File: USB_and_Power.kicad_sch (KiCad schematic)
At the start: 33 parts, among them J2 USB_C_Receptacle_USB2.0_14P, U2 TLV61070ADBV, U3 BQ24074RGT, U4 82400102, U5 TPS63031DSK, U6 FUSB303BTMX

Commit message: Added layout
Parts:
- removed J2: USB_C_Receptacle_USB2.0_14P, Connector_USB:USB_C_Receptacle_GCT_USB4105-xx-A_16P_TopMnt_Horizontal, symbol Connector:USB_C_Receptacle_USB2.0_14P
- added J6: USB_C_Receptacle_USB2.0_16P, Connector_USB:USB_C_Receptacle_GCT_USB4105-xx-A_16P_TopMnt_Horizontal, symbol Connector:USB_C_Receptacle_USB2.0_16P
- U2: footprint Package_DFN_QFN:Texas_RWU0007A_VQFN-7_2x2mm_P0.5mm -> TLV61070A:SOT95P280X145-6N
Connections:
- net GND: now also J6.A1 (GND), J6.A12 (GND), J6.B1 (GND), J6.B12 (GND)
- net VBUS: now also J6.A4 (VBUS), J6.A9 (VBUS), J6.B4 (VBUS), J6.B9 (VBUS)
- net at U6.1 (CC1): now also J6.A5 (CC1)
- net at U4.6: now also J6.A6 (D+), J6.B6 (D+)
- net at U4.4: now also J6.A7 (D-), J6.B7 (D-)
- net at U6.2 (CC2): now also J6.B5 (CC2)
- net at C17.1, R9.2: now also J6.S1 (SHIELD)
- no-connect marks 2 -> 4
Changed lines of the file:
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@@
 	)
 	(no_connect
+		(at 24.13 110.49)
+	)
+	(no_connect
 		(at 114.3 154.94)
 	)
 	(no_connect
+		(at 24.13 107.95)
+	)
+	(no_connect
 		(at 114.3 152.4)
 	)
@@
 	)
 	(symbol
-		(lib_id "power:GND")
-		(at 115.57 130.81 0)
+		(lib_name "USB_C_Receptacle_USB2.0_16P_1")
+		(lib_id "Connector:USB_C_Receptacle_USB2.0_16P")
+		(at 39.37 105.41 0)
 		(unit 1)
 		(exclude_from_sim no)
@@
 		(dnp no)
 		(fields_autoplaced yes)
-		(property "Reference" "#PWR020"
-			(at 115.57 137.16 0)
+		(property "Reference" "J6"
+			(at 39.37 74.93 0)
 			(effects
 				(font
 					(size 1.27 1.27)
 				)
-				(hide yes)
 			)
 		)
-		(property "Value" "GND"
-			(at 115.57 135.89 0)
+		(property "Value" "USB_C_Receptacle_USB2.0_16P"
+			(at 39.37 77.47 0)
 			(effects
 				(font
@@
 			)
 		)
-		(property "Footprint" ""
-			(at 115.57 130.81 0)
+		(property "Footprint" "Connector_USB:USB_C_Receptacle_GCT_USB4105-xx-A_16P_TopMnt_Horizontal"
+			(at 43.18 105.41 0)
 			(effects
 				(font
@@
 			)
 		)
-		(property "Datasheet" ""
-			(at 115.57 130.81 0)
+		(property "Datasheet" "https://www.usb.org/sites/default/files/documents/usb_type-c.zip"
+			(at 20.574 139.954 0)
 			(effects
 				(font
@@
 			)
 		)
-		(property "Description" "Power symbol creates a global label with name \"GND\" , ground"
-			(at 115.57 130.81 0)
+		(property "Description" "USB 2.0-only 16P Type-C Receptacle connector"
+			(at 39.37 114.3 0)
 			(effects
 				(font
@@
 			)
 		)
-		(pin "1"
+		(pin "B5"
+		)
+		(pin "A6"
+		)
+		(pin "A5"
+		)
+		(pin "A8"
+		)
+		(pin "B12"
+		)
+		(pin "A4"
+		)
+		(pin "A9"
+		)
+		(pin "B6"
+		)
+		(pin "B1"
+		)
+		(pin "A7"
+		)
+		(pin "S1"
+		)
+		(pin "B8"
+		)
+		(pin "B4"
+		)
+		(pin "B9"
+		)
+		(pin "A12"
+		)
+		(pin "B7"
+		)
+		(pin "A1"
 		)
 		(instances
 			(project "Snail_v1"
 				(path "/98695d9f-8521-4f7d-bb41-f22c1215a8e7/de25fb69-79bf-4de2-a7cc-36507c8760b8"
-					(reference "#PWR020")
+					(reference "J6")
 					(unit 1)
 				)
@@
 	(symbol
 		(lib_id "power:GND")
-		(at 142.24 68.58 0)
+		(at 115.57 130.81 0)
 		(unit 1)
 		(exclude_from_sim no)
@@
 		(dnp no)
 		(fields_autoplaced yes)
-		(property "Reference" "#PWR012"
-			(at 142.24 74.93 0)
+		(property "Reference" "#PWR020"
+			(at 115.57 137.16 0)
 			(effects
 				(font
@@
 		)
 		(property "Value" "GND"
-			(at 142.24 73.66 0)
+			(at 115.57 135.89 0)
 			(effects
 				(font
@@
 		)
 		(property "Footprint" ""
-			(at 142.24 68.58 0)
+			(at 115.57 130.81 0)
 			(effects
 				(font
@@
 		)
 		(property "Datasheet" ""
-			(at 142.24 68.58 0)
+			(at 115.57 130.81 0)
 			(effects
 				(font
@@
 		)
 		(property "Description" "Power symbol creates a global label with name \"GND\" , ground"
-			(at 142.24 68.58 0)
+			(at 115.57 130.81 0)
 			(effects
 				(font
@@
 			(project "Snail_v1"
 				(path "/98695d9f-8521-4f7d-bb41-f22c1215a8e7/de25fb69-79bf-4de2-a7cc-36507c8760b8"
-					(reference "#PWR012")
+					(reference "#PWR020")
 					(unit 1)
 				)
@@
 	)
 	(symbol
-		(lib_id "Device:C_Small")
-		(at 73.66 88.9 0)
-		(mirror x)
+		(lib_id "power:GND")
+		(at 142.24 68.58 0)
 		(unit 1)
 		(exclude_from_sim no)
@@
 		(dnp no)
 		(fields_autoplaced yes)
-		(property "Reference" "C10"
-			(at 71.12 87.6235 0)
+		(property "Reference" "#PWR012"
+			(at 142.24 74.93 0)
 			(effects
 				(font
 					(size 1.27 1.27)
 				)
-				(justify right)
+				(hide yes)
 			)
 		)
-		(property "Value" "1uF"
-			(at 71.12 90.1635 0)
+		(property "Value" "GND"
+			(at 142.24 73.66 0)
 			(effects
 				(font
 					(size 1.27 1.27)
 				)
-				(justify right)
 			)
 		)
-		(property "Footprint" "Capacitor_SMD:C_0805_2012Metric_Pad1.18x1.45mm_HandSolder"
-			(at 73.66 88.9 0)
+		(property "Footprint" ""
+			(at 142.24 68.58 0)
 			(effects
 				(font
@@
 			)
 		)
-		(property "Datasheet" "~"
-			(at 73.66 88.9 0)
+		(property "Datasheet" ""
+			(at 142.24 68.58 0)
 			(effects
 				(font
@@
 			)
 		)
-		(property "Description" "Unpolarized capacitor, small symbol"
-			(at 73.66 88.9 0)
+		(property "Description" "Power symbol creates a global label with name \"GND\" , ground"
+			(at 142.24 68.58 0)
 			(effects
 				(font
@@
 			)
 		)
-		(pin "2"
-		)
 		(pin "1"
 		)
@@
 			(project "Snail_v1"
 				(path "/98695d9f-8521-4f7d-bb41-f22c1215a8e7/de25fb69-79bf-4de2-a7cc-36507c8760b8"
-					(reference "C10")
+					(reference "#PWR012")
 					(unit 1)
 				)
@@
 	)
 	(symbol
-		(lib_id "Connector:USB_C_Receptacle_USB2.0_14P")
-		(at 39.37 105.41 0)
+		(lib_id "Device:C_Small")
+		(at 73.66 88.9 0)
+		(mirror x)
 		(unit 1)
 		(exclude_from_sim no)
@@
 		(on_board yes)
 		(dnp no)
-		(property "Reference" "J2"
-			(at 39.37 75.946 0)
+		(fields_autoplaced yes)
+		(property "Reference" "C10"
+			(at 71.12 87.6235 0)
 			(effects
 				(font
 					(size 1.27 1.27)
 				)
+				(justify right)
 			)
 		)
-		(property "Value" "USB_C_Receptacle_USB2.0_14P"
-			(at 39.37 78.486 0)
+		(property "Value" "1uF"
+			(at 71.12 90.1635 0)
 			(effects
 				(font
 					(size 1.27 1.27)
 				)
+				(justify right)
 			)
 		)
-		(property "Footprint" "Connector_USB:USB_C_Receptacle_GCT_USB4105-xx-A_16P_TopMnt_Horizontal"
-			(at 43.18 105.41 0)
+		(property "Footprint" "Capacitor_SMD:C_0805_2012Metric_Pad1.18x1.45mm_HandSolder"
+			(at 73.66 88.9 0)
 			(effects
 				(font
@@
 			)
 		)
-		(property "Datasheet" "https://www.usb.org/sites/default/files/documents/usb_type-c.zip"
-			(at 43.18 106.68 0)
+		(property "Datasheet" "~"
+			(at 73.66 88.9 0)
 			(effects
 				(font
@@
 			)
 		)
-		(property "Description" "USB 2.0-only 14P Type-C Receptacle connector"
-			(at 39.37 106.68 0)
+		(property "Description" "Unpolarized capacitor, small symbol"
+			(at 73.66 88.9 0)
 			(effects
 				(font
@@
 			)
 		)
-		(pin "B7"
-		)
-		(pin "B6"
-		)
-		(pin "S1"
-		)
-		(pin "A1"
-		)
-		(pin "A4"
-		)
-		(pin "A9"
-		)
-		(pin "B4"
-		)
-		(pin "A7"
-		)
-		(pin "B1"
-		)
-		(pin "B12"
-		)
-		(pin "B9"
-		)
-		(pin "A5"
-		)
-		(pin "B5"
-		)
-		(pin "A12"
+		(pin "2"
 		)
-		(pin "A6"
+		(pin "1"
 		)
 		(instances
 			(project "Snail_v1"
 				(path "/98695d9f-8521-4f7d-bb41-f22c1215a8e7/de25fb69-79bf-4de2-a7cc-36507c8760b8"
-					(reference "J2")
+					(reference "C10")
 					(unit 1)
 				)
@@
 			)
 		)
-		(property "Footprint" "Package_DFN_QFN:Texas_RWU0007A_VQFN-7_2x2mm_P0.5mm"
+		(property "Footprint" "TLV61070A:SOT95P280X145-6N"
 			(at 228.6 58.42 0)
 			(effects

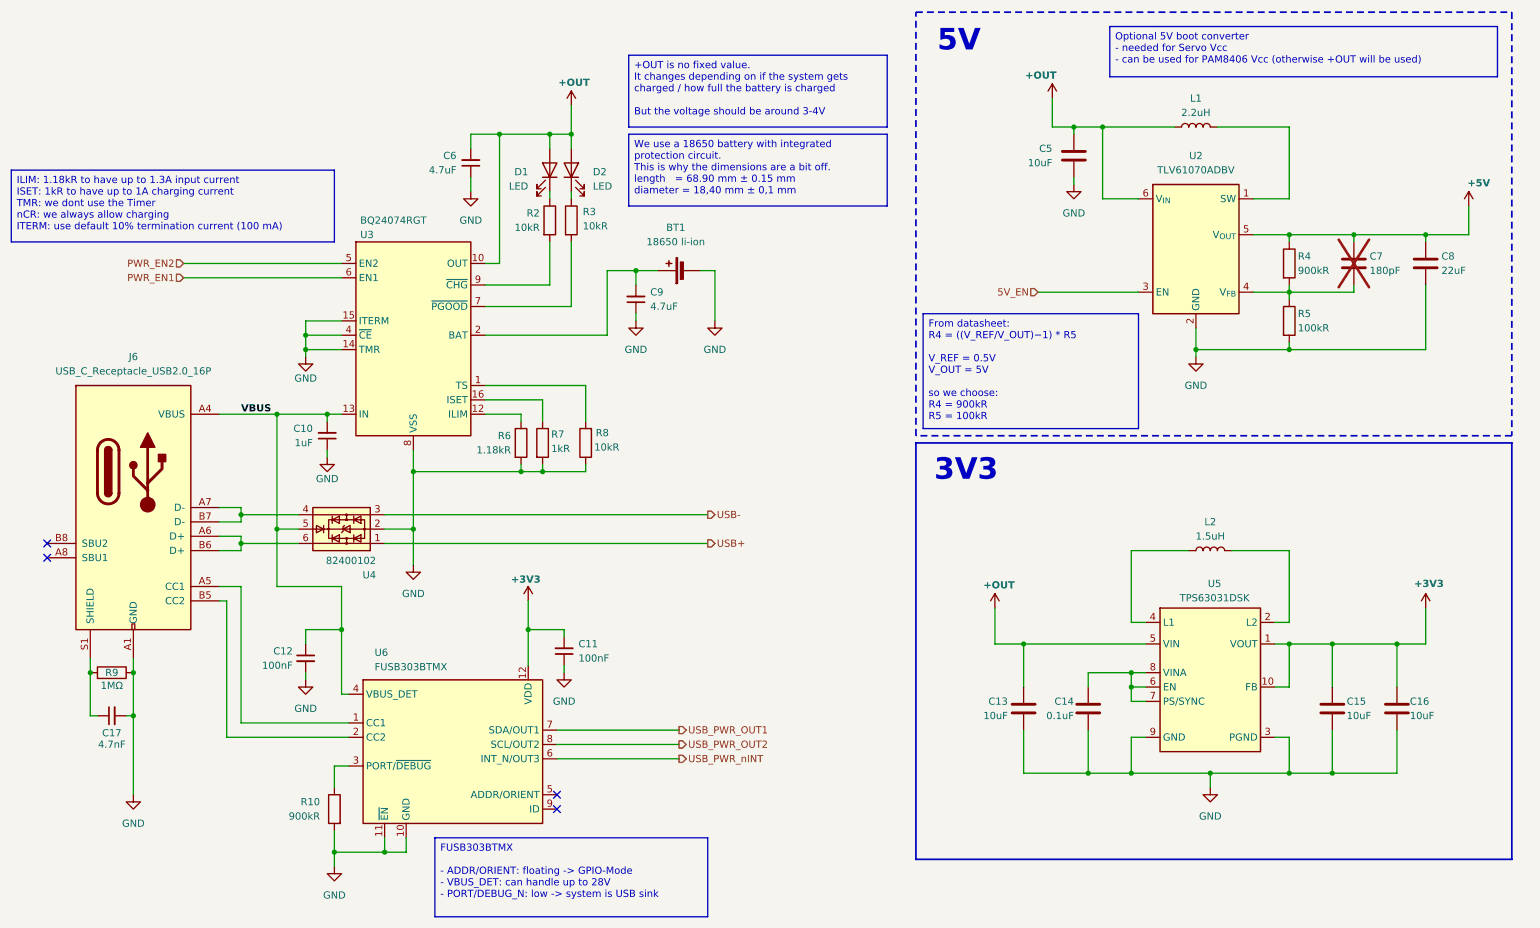
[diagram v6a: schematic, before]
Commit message: Did Silkscreen + added images of PCBA
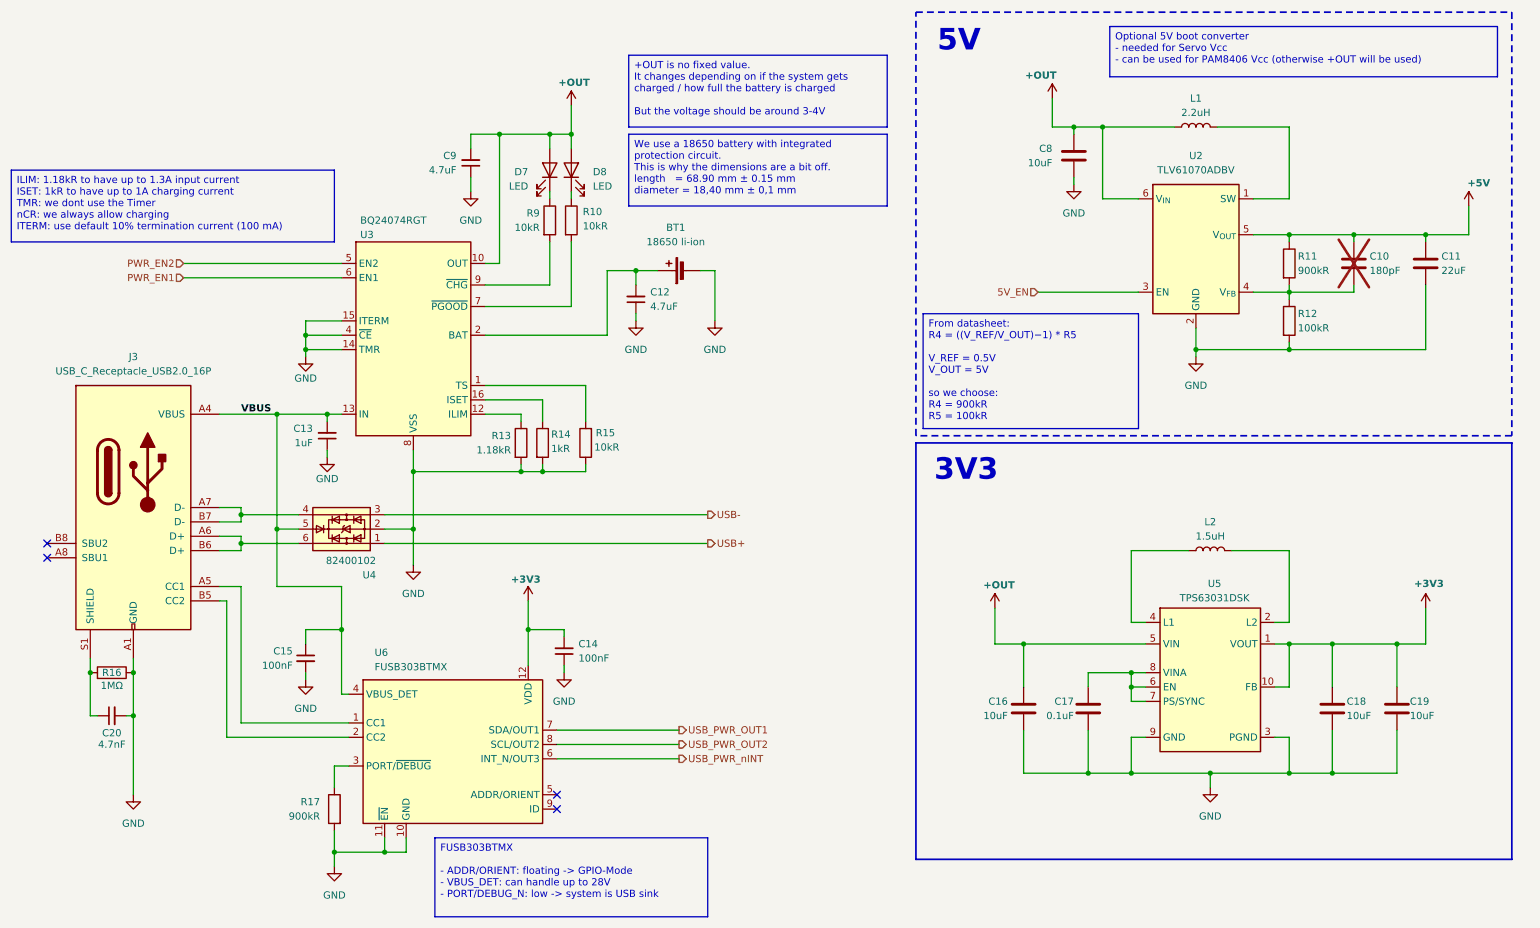
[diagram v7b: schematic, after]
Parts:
- renumbered C7 to C10, C8 to C11, C9 to C12, C10 to C13, C11 to C14, C12 to C15, C13 to C16, C14 to C17, C15 to C18, C16 to C19, C17 to C20, C5 to C8, C6 to C9, D1 to D7, D2 to D8, J6 to J3, R3 to R10, R4 to R11, R5 to R12, R6 to R13, R7 to R14, R8 to R15, R9 to R16, R10 to R17, R2 to R9

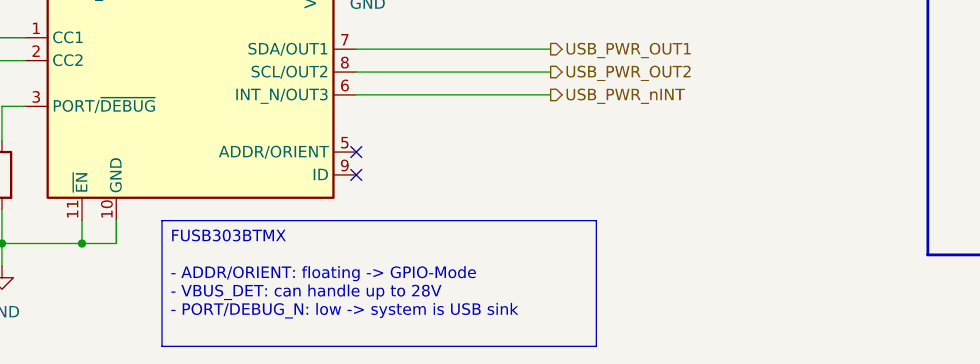
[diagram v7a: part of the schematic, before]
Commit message: Added missing AMP_nSD connection to MCU via 5V_EN
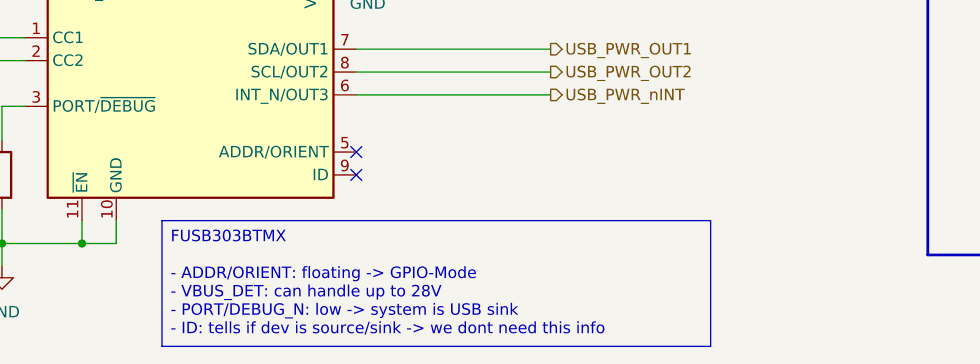
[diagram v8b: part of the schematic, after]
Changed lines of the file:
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@@
 		)
 	)
-	(text_box "FUSB303BTMX\n\n- ADDR/ORIENT: floating -> GPIO-Mode\n- VBUS_DET: can handle up to 28V\n- PORT/DEBUG_N: low -> system is USB sink"
+	(text_box "FUSB303BTMX\n\n- ADDR/ORIENT: floating -> GPIO-Mode\n- VBUS_DET: can handle up to 28V\n- PORT/DEBUG_N: low -> system is USB sink\n- ID: tells if dev is source/sink -> we dont need this info"
 		(exclude_from_sim no)
 		(at 92.71 160.02 0)
-		(size 48.26 13.97)
+		(size 60.96 13.97)
 		(margins 0.9525 0.9525 0.9525 0.9525)
 		(stroke
